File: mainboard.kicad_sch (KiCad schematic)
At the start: 27 parts, among them J1 DRV8833-1, J2 DRV8833-0, J3 Conn_01x02, J4 Screw_Terminal_01x06, J5 Screw_Terminal_01x06, J6 VIM4_HEADER, J7 Conn_01x02, J8 Conn_01x02, Q1 2N7000, Q2 2N7000, SW1 RotaryEncoder_Switch, U1 MCP23017_SP

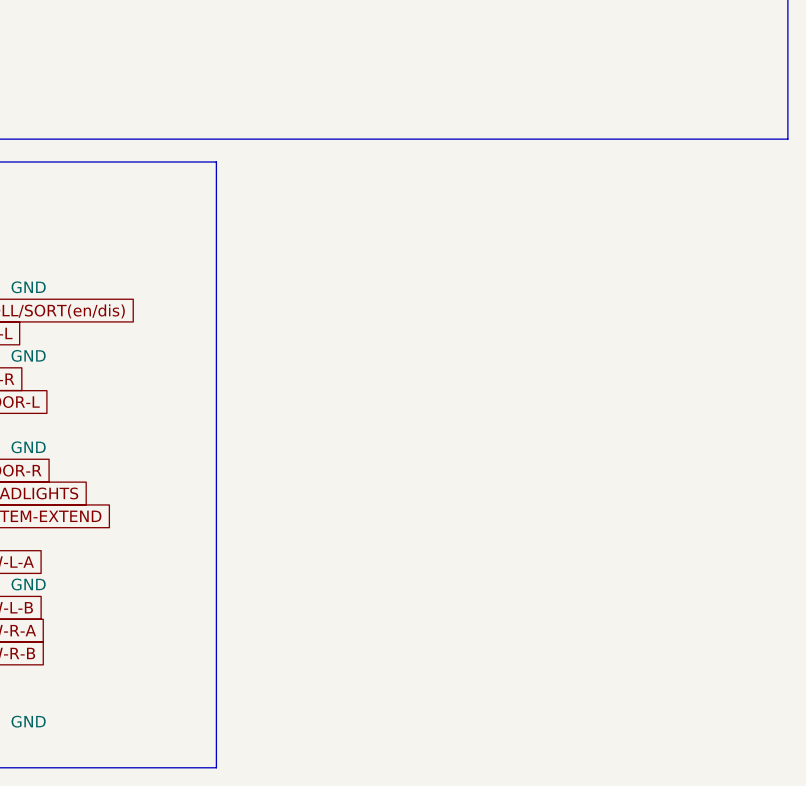
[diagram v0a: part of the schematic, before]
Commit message: Added LDR circuit
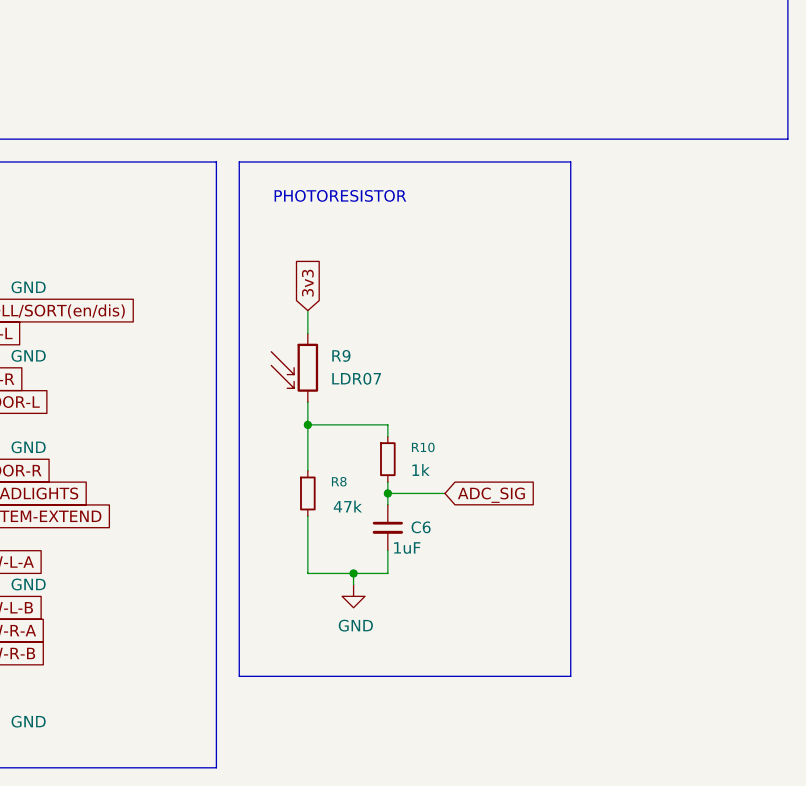
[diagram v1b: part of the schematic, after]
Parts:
- added C6: 1uF, symbol Device:C_Small
- added R10: 1k, symbol Device:R_Small
- added R8: 47k, symbol Device:R_Small
- added R9: LDR07, OptoDevice:R_LDR_5.1x4.3mm_P3.4mm_Vertical, symbol Sensor_Optical:LDR07
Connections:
- net 3v3: now also R9.1
- net GND: now also C6.2, R8.2
- new net: R10.1, R8.1, R9.2
- new net ADC_SIG: C6.1, R10.2
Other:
- note added: "PHOTORESISTOR"

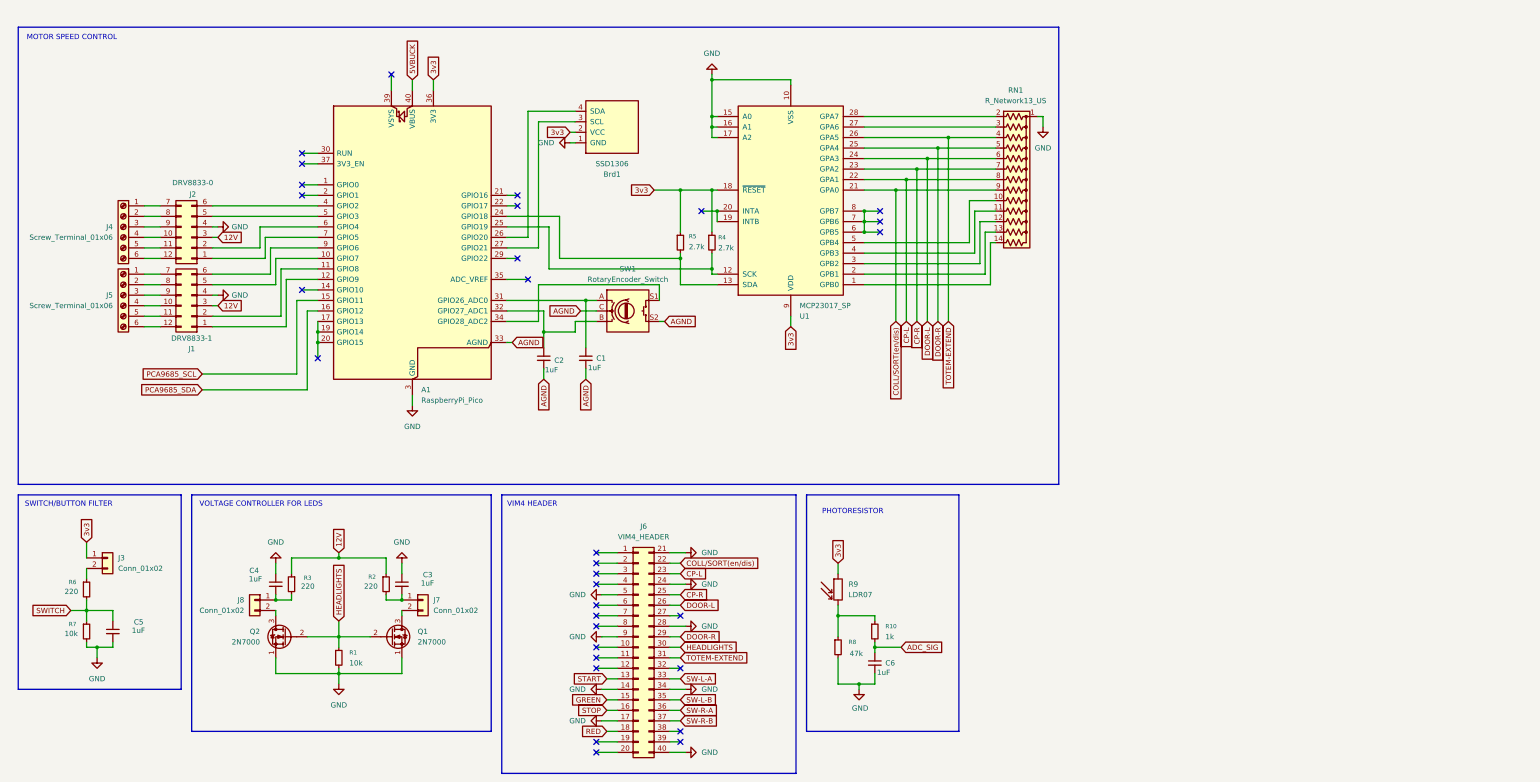
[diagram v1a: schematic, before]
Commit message: Bucks added
Bucks added, nets modified to match these buck names
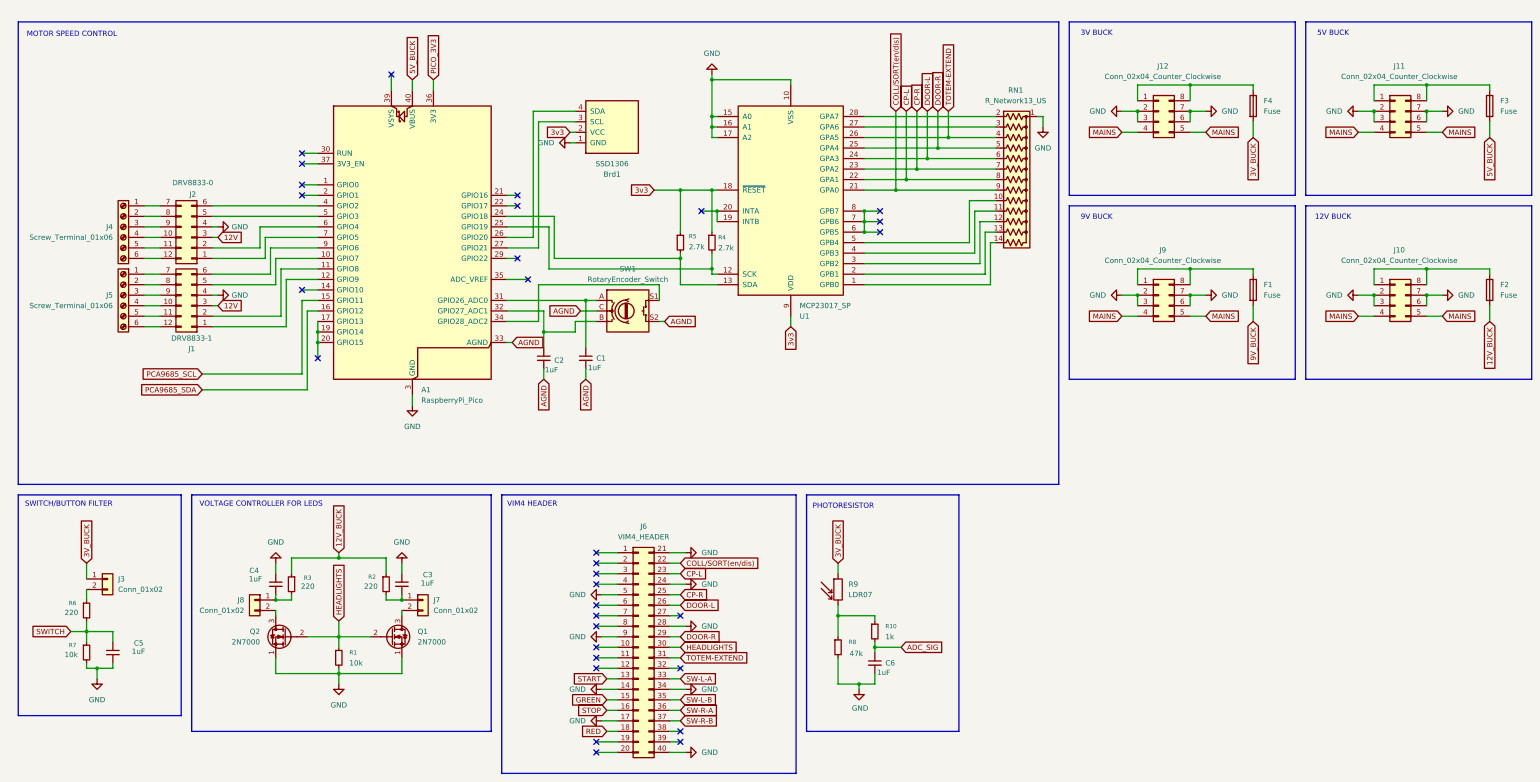
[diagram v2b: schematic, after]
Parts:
- added F1, F2, F3, F4: Fuse, symbol Device:Fuse
- added J10, J11, J12, J9: Conn_02x04_Counter_Clockwise, symbol Connector_Generic:Conn_02x04_Counter_Clockwise
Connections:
- net 12V: no longer R2.1, R3.1
- net 3v3: no longer A1.36 (3V3), J3.1 (Pin_1), R9.1
- net GND: now also J10.2 (Pin_2), J10.3 (Pin_3), J10.6 (Pin_6), J10.7 (Pin_7), J11.2 (Pin_2), J11.3 (Pin_3), J11.6 (Pin_6), J11.7 (Pin_7), J12.2 (Pin_2), J12.3 (Pin_3), J12.6 (Pin_6), J12.7 (Pin_7), J9.2 (Pin_2), J9.3 (Pin_3), J9.6 (Pin_6), J9.7 (Pin_7)
- net 5VBUCK renamed 5V_BUCK
- net 5V_BUCK: now also F3.2
- new net: F4.1, J12.1 (Pin_1), J12.8 (Pin_8)
- new net: F3.1, J11.1 (Pin_1), J11.8 (Pin_8)
- new net: F1.1, J9.1 (Pin_1), J9.8 (Pin_8)
- new net: F2.1, J10.1 (Pin_1), J10.8 (Pin_8)
- new net 12V_BUCK: F2.2, R2.1, R3.1
- new net 3V_BUCK: F4.2, J3.1 (Pin_1), R9.1
- new net 9V_BUCK: F1.2
- new net MAINS: J10.4 (Pin_4), J10.5 (Pin_5), J11.4 (Pin_4), J11.5 (Pin_5), J12.4 (Pin_4), J12.5 (Pin_5), J9.4 (Pin_4), J9.5 (Pin_5)
- new net PICO_3V3: A1.36 (3V3)
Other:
- note added: "12V BUCK"
- note added: "3V BUCK"
- note added: "5V BUCK"
- note added: "9V BUCK"
- moved on the sheet: C5, J3, R6, R7

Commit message: Added PCB
Added PCB and DRV8833 footprint.
Error checked circuit for footprints to PCB
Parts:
- Brd1: footprint (none) -> Connector_Molex:Molex_KK-254_AE-6410-04A_1x04_P2.54mm_Vertical
- C1, C2, C3, C4, C5, C6: footprint (none) -> Capacitor_SMD:C_0805_2012Metric
- F1, F2, F3, F4: footprint (none) -> Fuse:Fuseholder_Clip-5x20mm_Schurter_CQM_Inline_P20.60x5.00mm_D1.00mm_Horizontal
- J1, J2: footprint Connector_PinHeader_2.54mm:PinHeader_2x05_P2.54mm_Vertical_SMD -> Library:DRV8833
- J10, J11, J12, J9: footprint (none) -> Connector_PinHeader_2.54mm:PinHeader_2x04_P2.54mm_Vertical
- J3, J7, J8: footprint (none) -> Connector_PinHeader_2.54mm:PinHeader_1x02_P2.54mm_Vertical
- J4, J5: footprint Connector_Phoenix_MC:PhoenixContact_MCV_1,5_6-GF-3.5_1x06_P3.50mm_Vertical_ThreadedFlange_MountHole -> TerminalBlock:TerminalBlock_Xinya_XY308-2.54-6P_1x06_P2.54mm_Horizontal
- J6: footprint (none) -> Connector_PinHeader_2.54mm:PinHeader_2x20_P2.54mm_Vertical
- R1, R10, R2, R3, R4, R5, R6, R7, R8: footprint (none) -> Resistor_SMD:R_0805_2012Metric
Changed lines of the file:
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@@
 			)
 		)
-		(property "Footprint" ""
+		(property "Footprint" "Capacitor_SMD:C_0805_2012Metric"
 			(at 219.71 168.91 0)
 			(effects
@@
 			)
 		)
-		(property "Footprint" ""
+		(property "Footprint" "Capacitor_SMD:C_0805_2012Metric"
 			(at 35.56 166.37 0)
 			(effects
@@
 			)
 		)
-		(property "Footprint" ""
+		(property "Footprint" "Connector_PinHeader_2.54mm:PinHeader_1x02_P2.54mm_Vertical"
 			(at 34.29 148.59 0)
 			(effects
@@
 			)
 		)
-		(property "Footprint" ""
+		(property "Footprint" "Resistor_SMD:R_0805_2012Metric"
 			(at 180.34 67.31 0)
 			(effects
@@
 			)
 		)
-		(property "Footprint" ""
+		(property "Footprint" "Connector_PinHeader_2.54mm:PinHeader_2x20_P2.54mm_Vertical"
 			(at 162.56 165.1 0)
 			(effects
@@
 			)
 		)
-		(property "Footprint" ""
+		(property "Footprint" "Resistor_SMD:R_0805_2012Metric"
 			(at 29.21 156.21 0)
 			(effects
@@
 			)
 		)
-		(property "Footprint" ""
+		(property "Footprint" "Connector_Molex:Molex_KK-254_AE-6410-04A_1x04_P2.54mm_Vertical"
 			(at 149.86 39.37 0)
 			(effects
@@
 			)
 		)
-		(property "Footprint" ""
+		(property "Footprint" "Resistor_SMD:R_0805_2012Metric"
 			(at 78.74 149.86 0)
 			(effects
@@
 			)
 		)
-		(property "Footprint" "Connector_PinHeader_2.54mm:PinHeader_2x05_P2.54mm_Vertical_SMD"
+		(property "Footprint" "Library:DRV8833"
 			(at 54.61 82.55 0)
 			(effects
@@
 			)
 		)
-		(property "Footprint" ""
+		(property "Footprint" "Resistor_SMD:R_0805_2012Metric"
 			(at 101.6 149.86 0)
 			(effects
@@
 			)
 		)
-		(property "Footprint" ""
+		(property "Footprint" "Capacitor_SMD:C_0805_2012Metric"
 			(at 74.93 149.86 0)
 			(effects
@@
 			)
 		)
-		(property "Footprint" ""
+		(property "Footprint" "Connector_PinHeader_2.54mm:PinHeader_2x04_P2.54mm_Vertical"
 			(at 288.29 35.56 0)
 			(effects
@@
 			)
 		)
-		(property "Footprint" ""
+		(property "Footprint" "Capacitor_SMD:C_0805_2012Metric"
 			(at 105.41 149.86 0)
 			(effects
@@
 			)
 		)
-		(property "Footprint" ""
+		(property "Footprint" "Connector_PinHeader_2.54mm:PinHeader_2x04_P2.54mm_Vertical"
 			(at 345.44 35.56 0)
 			(effects
@@
 			)
 		)
-		(property "Footprint" ""
+		(property "Footprint" "Fuse:Fuseholder_Clip-5x20mm_Schurter_CQM_Inline_P20.60x5.00mm_D1.00mm_Horizontal"
 			(at 309.372 78.74 90)
 			(effects
@@
 			)
 		)
-		(property "Footprint" ""
+		(property "Footprint" "Capacitor_SMD:C_0805_2012Metric"
 			(at 149.86 95.25 0)
 			(effects
@@
 			)
 		)
-		(property "Footprint" ""
+		(property "Footprint" "Fuse:Fuseholder_Clip-5x20mm_Schurter_CQM_Inline_P20.60x5.00mm_D1.00mm_Horizontal"
 			(at 366.522 78.74 90)
 			(effects
@@
 			)
 		)
-		(property "Footprint" ""
+		(property "Footprint" "Resistor_SMD:R_0805_2012Metric"
 			(at 29.21 166.37 0)
 			(effects
@@
 			)
 		)
-		(property "Footprint" ""
+		(property "Footprint" "Fuse:Fuseholder_Clip-5x20mm_Schurter_CQM_Inline_P20.60x5.00mm_D1.00mm_Horizontal"
 			(at 309.372 34.29 90)
 			(effects
@@
 			)
 		)
-		(property "Footprint" ""
+		(property "Footprint" "Resistor_SMD:R_0805_2012Metric"
 			(at 90.17 167.64 0)
 			(effects
@@
 			)
 		)
-		(property "Footprint" ""
+		(property "Footprint" "Connector_PinHeader_2.54mm:PinHeader_2x04_P2.54mm_Vertical"
 			(at 345.44 80.01 0)
 			(effects
@@
 			)
 		)
-		(property "Footprint" "Connector_Phoenix_MC:PhoenixContact_MCV_1,5_6-GF-3.5_1x06_P3.50mm_Vertical_ThreadedFlange_MountHole"
+		(property "Footprint" "TerminalBlock:TerminalBlock_Xinya_XY308-2.54-6P_1x06_P2.54mm_Horizontal"
 			(at 38.1 80.01 0)
 			(effects
@@
 			)
 		)
-		(property "Footprint" ""
+		(property "Footprint" "Resistor_SMD:R_0805_2012Metric"
 			(at 172.72 67.31 0)
 			(effects
@@
 			)
 		)
-		(property "Footprint" ""
+		(property "Footprint" "Connector_PinHeader_2.54mm:PinHeader_1x02_P2.54mm_Vertical"
 			(at 69.85 153.67 0)
 			(effects
@@
 			)
 		)
-		(property "Footprint" ""
+		(property "Footprint" "Capacitor_SMD:C_0805_2012Metric"
 			(at 139.7 95.25 0)
 			(effects
@@
 			)
 		)
-		(property "Footprint" ""
+		(property "Footprint" "Connector_PinHeader_2.54mm:PinHeader_1x02_P2.54mm_Vertical"
 			(at 110.49 153.67 0)
 			(effects
@@
 			)
 		)
-		(property "Footprint" "Connector_Phoenix_MC:PhoenixContact_MCV_1,5_6-GF-3.5_1x06_P3.50mm_Vertical_ThreadedFlange_MountHole"
+		(property "Footprint" "TerminalBlock:TerminalBlock_Xinya_XY308-2.54-6P_1x06_P2.54mm_Horizontal"
 			(at 38.1 63.5 0)
 			(effects
@@
 			)
 		)
-		(property "Footprint" "Connector_PinHeader_2.54mm:PinHeader_2x05_P2.54mm_Vertical_SMD"
+		(property "Footprint" "Library:DRV8833"
 			(at 54.61 66.04 0)
 			(effects
@@
 			)
 		)
-		(property "Footprint" ""
+		(property "Footprint" "Connector_PinHeader_2.54mm:PinHeader_2x04_P2.54mm_Vertical"
 			(at 288.29 80.01 0)
 			(effects
@@
 			)
 		)
-		(property "Footprint" ""
+		(property "Footprint" "Resistor_SMD:R_0805_2012Metric"
 			(at 219.71 161.29 0)
 			(effects
@@
 			)
 		)
-		(property "Footprint" ""
+		(property "Footprint" "Fuse:Fuseholder_Clip-5x20mm_Schurter_CQM_Inline_P20.60x5.00mm_D1.00mm_Horizontal"
 			(at 366.522 34.29 90)
 			(effects
@@
 			)
 		)
-		(property "Footprint" ""
+		(property "Footprint" "Resistor_SMD:R_0805_2012Metric"
 			(at 210.82 165.1 0)
 			(effects

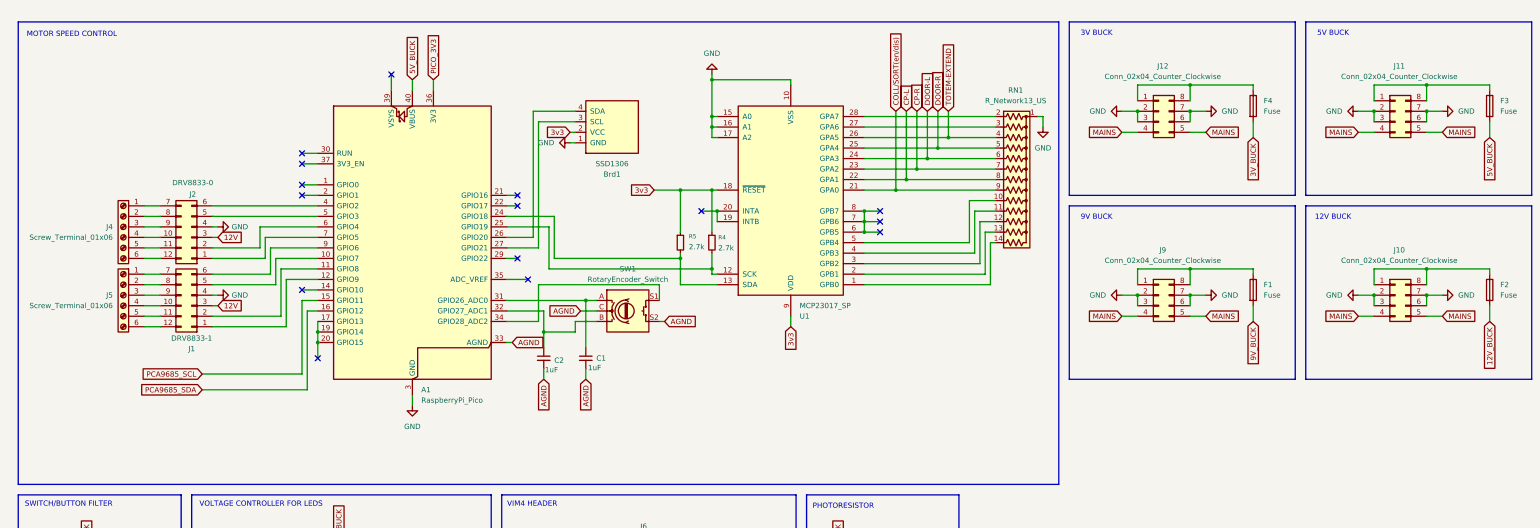
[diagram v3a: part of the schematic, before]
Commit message: Settings import
Imported settings for traces and routing,
Placing and organizing PCB components into modules
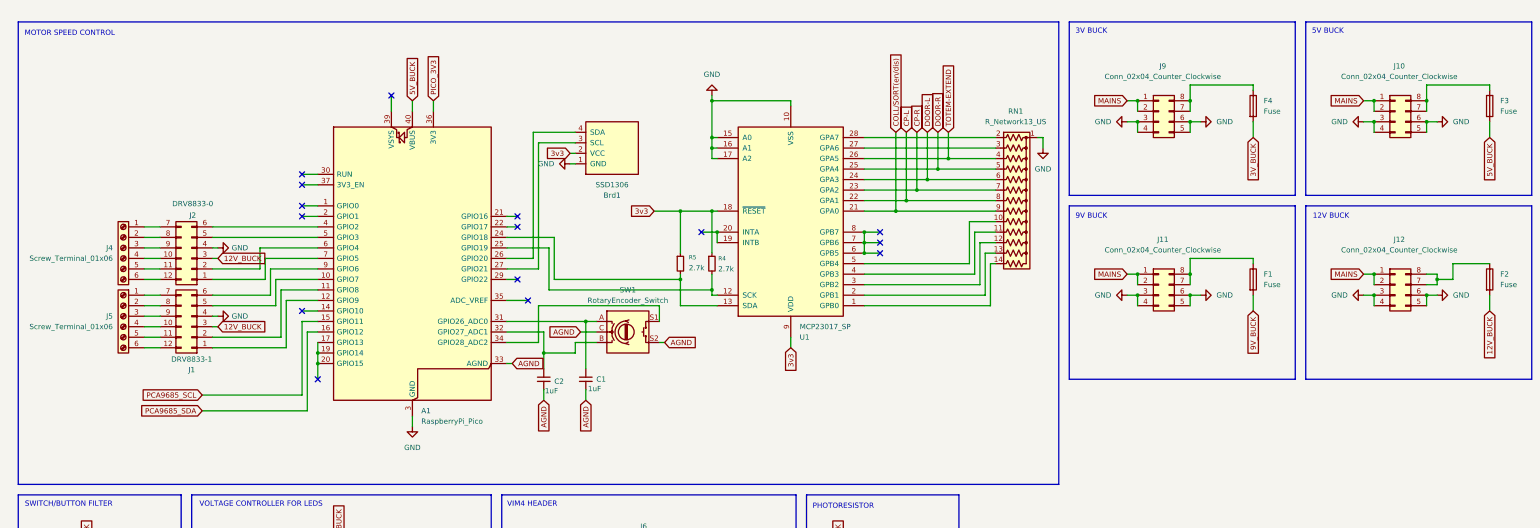
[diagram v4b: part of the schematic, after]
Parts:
- removed J9: Conn_02x04_Counter_Clockwise, Connector_PinHeader_2.54mm:PinHeader_2x04_P2.54mm_Vertical, symbol Connector_Generic:Conn_02x04_Counter_Clockwise
- added J12: Conn_02x04_Counter_Clockwise, Connector_PinHeader_2.54mm:PinHeader_2x04_P2.54mm_Vertical, symbol Connector_Generic:Conn_02x04_Counter_Clockwise
- renumbered J12 to J9
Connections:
- net 12V is gone; now on net 12V_BUCK: J1.3 (Pin_3), J2.3 (Pin_3)
- net GND: now also J10.4 (Pin_4), J10.5 (Pin_5), J11.4 (Pin_4), J11.5 (Pin_5), J9.4 (Pin_4), J9.5 (Pin_5), J12.3 (Pin_3), J12.4 (Pin_4), J12.5 (Pin_5), J12.6 (Pin_6); no longer J10.2 (Pin_2), J10.7 (Pin_7), J11.2 (Pin_2), J11.7 (Pin_7), J9.2 (Pin_2), J9.7 (Pin_7)
- net MAINS: now also J10.1 (Pin_1), J10.2 (Pin_2), J11.1 (Pin_1), J11.2 (Pin_2), J9.1 (Pin_1), J9.2 (Pin_2), J12.1 (Pin_1), J12.2 (Pin_2); no longer J10.4 (Pin_4), J10.5 (Pin_5), J11.4 (Pin_4), J11.5 (Pin_5), J9.4 (Pin_4), J9.5 (Pin_5)
- net at F4.1, J9.8 (Pin_8): now also J9.7 (Pin_7); no longer J9.1 (Pin_1)
- net at F1.1: now also J11.7 (Pin_7), J11.8 (Pin_8)
- new net: F2.1, J12.7 (Pin_7), J12.8 (Pin_8)
- new net: F3.1, J10.7 (Pin_7), J10.8 (Pin_8)
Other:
- moved on the sheet: A1, Brd1, C1, C2, J1, J2, J4, J5, R4, R5, RN1, SW1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
